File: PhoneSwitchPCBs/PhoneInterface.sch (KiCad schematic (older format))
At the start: 52 parts

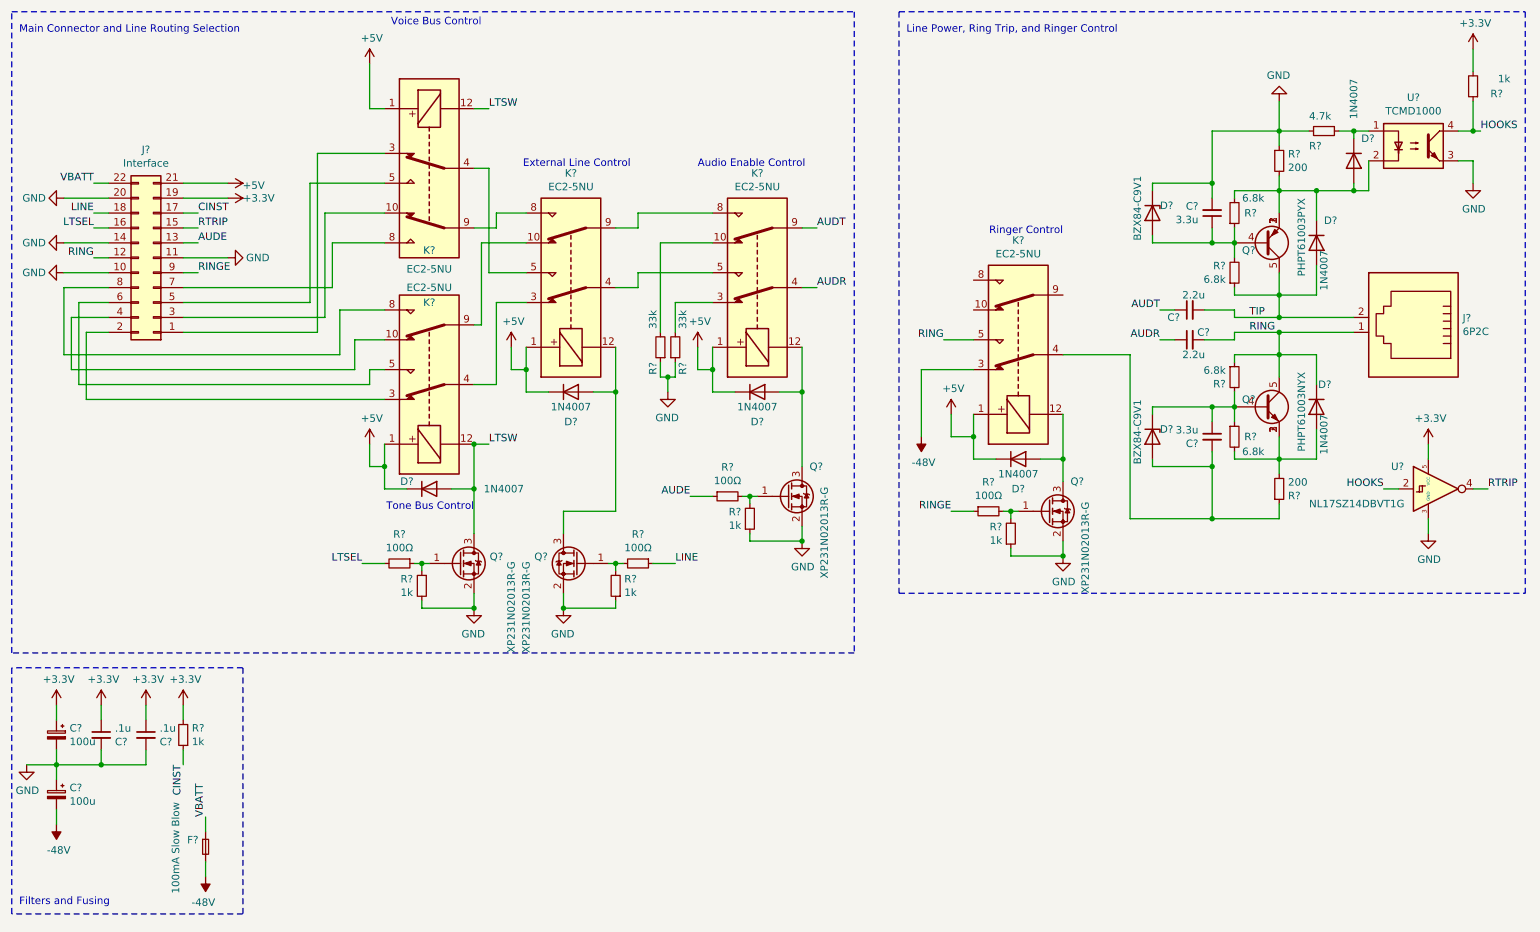
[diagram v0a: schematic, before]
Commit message: Update Notes, create custom footprint for RJ11 connector, associate footprints, fix cap types
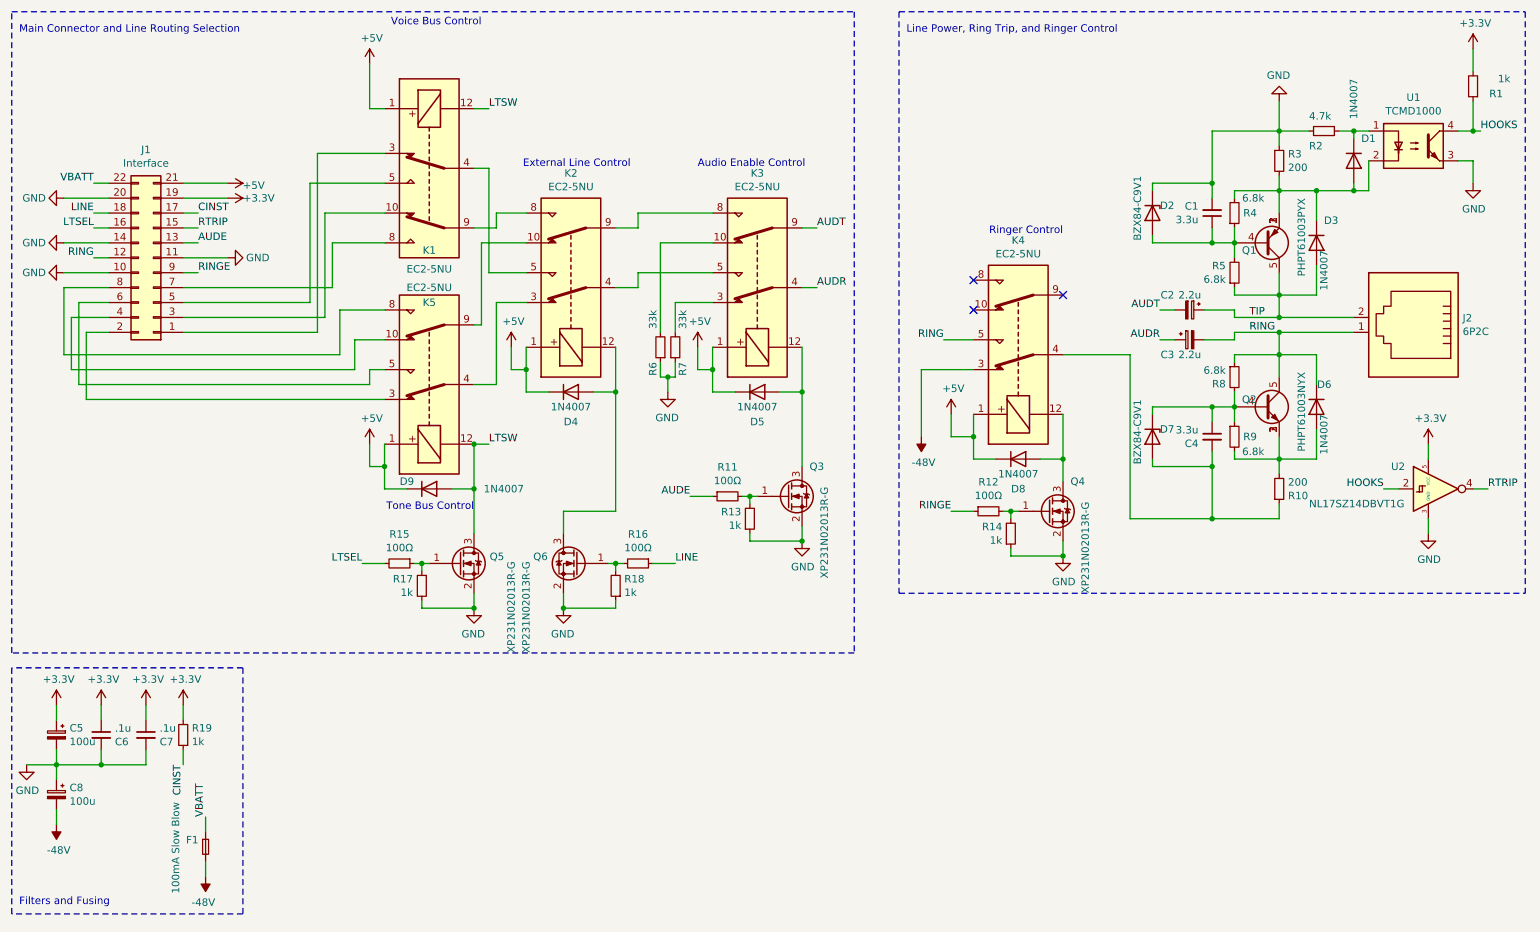
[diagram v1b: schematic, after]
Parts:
- removed C? (x2): 2.2u, symbol Device:C_Small
- added C2, C3: 2.2u, Capacitor_THT:CP_Radial_D4.0mm_P1.50mm, symbol Device:CP_Small
- C1, C4, C5: renamed from C?; footprint (none) -> Capacitor_THT:CP_Radial_D5.0mm_P2.00mm
- C8: renamed from C?; footprint (none) -> Capacitor_THT:CP_Radial_D10.0mm_P5.00mm
- F1: renamed from F?; footprint (none) -> Imported_Parts:00346605
- J1: renamed from J?; footprint (none) -> Connector_PinHeader_2.54mm:PinHeader_2x11_P2.54mm_Vertical
- J2: renamed from J?; footprint (none) -> PhoneInterfaceParts:RJE0112001
- R1, R13, R14, R17, R18, R19: renamed from R?; footprint (none) -> Resistor_SMD:R_0805_2012Metric_Pad1.20x1.40mm_HandSolder
- R4, R5, R8, R9: renamed from R?; footprint (none) -> Resistor_SMD:R_1210_3225Metric_Pad1.30x2.65mm_HandSolder
- gave numbers to parts that had none: 33
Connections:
- net AUDR: now also C3.1
- net AUDT: now also C2.2
- net RING: now also C3.2
- net TIP: now also C2.1
- no-connect marks 0 -> 3

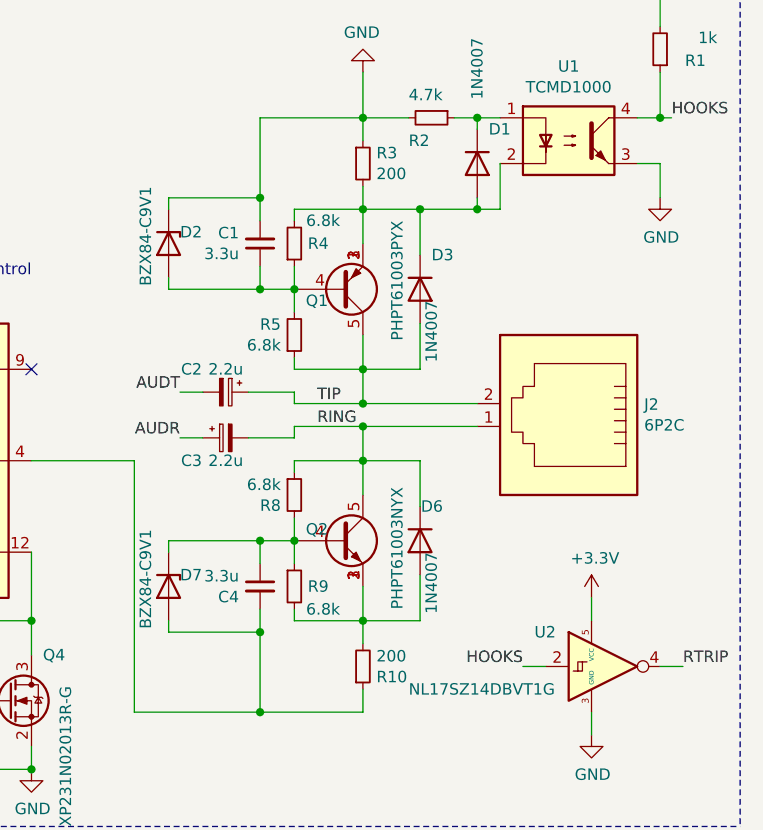
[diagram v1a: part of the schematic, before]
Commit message: Finished footprint associations
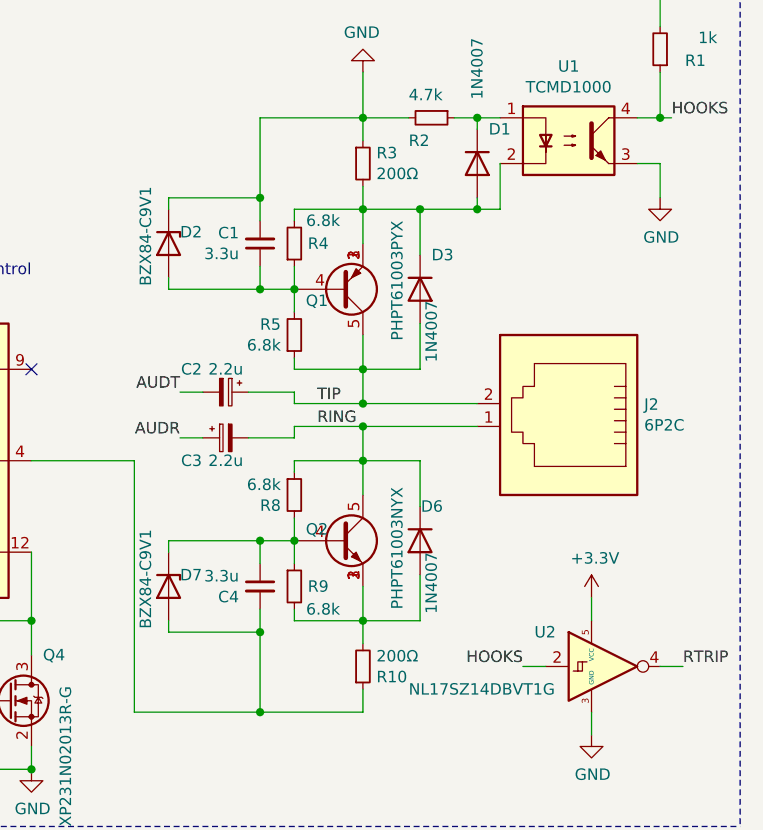
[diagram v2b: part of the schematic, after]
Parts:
- C6, C7: footprint (none) -> Capacitor_SMD:C_0603_1608Metric_Pad1.08x0.95mm_HandSolder
- R10, R3: value 200 -> 200Ω; footprint (none) -> Resistor_THT:R_Axial_DIN0516_L15.5mm_D5.0mm_P20.32mm_Horizontal
- R11, R12, R15, R16, R2, R6, R7: footprint (none) -> Resistor_SMD:R_0805_2012Metric_Pad1.20x1.40mm_HandSolder
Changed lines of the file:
@@
 P 9250 1650
 F 0 "R3" H 9309 1696 50  0000 L CNN
-F 1 "200" H 9309 1605 50  0000 L CNN
-F 2 "" H 9250 1650 50  0001 C CNN
+F 1 "200Ω" H 9309 1605 50  0000 L CNN
+F 2 "Resistor_THT:R_Axial_DIN0516_L15.5mm_D5.0mm_P20.32mm_Horizontal" H 9250 1650 50  0001 C CNN
 F 3 "~" H 9250 1650 50  0001 C CNN
 	1    9250 1650
@@
 P 9250 3850
 F 0 "R10" H 9309 3896 50  0000 L CNN
-F 1 "200" H 9309 3805 50  0000 L CNN
-F 2 "" H 9250 3850 50  0001 C CNN
+F 1 "200Ω" H 9309 3805 50  0000 L CNN
+F 2 "Resistor_THT:R_Axial_DIN0516_L15.5mm_D5.0mm_P20.32mm_Horizontal" H 9250 3850 50  0001 C CNN
 F 3 "~" H 9250 3850 50  0001 C CNN
 	1    9250 3850
@@
 F 0 "R2" V 9650 1350 50  0000 L CNN
 F 1 "4.7k" V 9450 1350 50  0000 L CNN
-F 2 "" H 9550 1450 50  0001 C CNN
+F 2 "Resistor_SMD:R_0805_2012Metric_Pad1.20x1.40mm_HandSolder" H 9550 1450 50  0001 C CNN
 F 3 "~" H 9550 1450 50  0001 C CNN
 	1    9550 1450
@@
 F 0 "R7" V 5250 3000 50  0000 L CNN
 F 1 "33k" V 5250 2650 50  0000 L CNN
-F 2 "" H 5200 2900 50  0001 C CNN
+F 2 "Resistor_SMD:R_0805_2012Metric_Pad1.20x1.40mm_HandSolder" H 5200 2900 50  0001 C CNN
 F 3 "~" H 5200 2900 50  0001 C CNN
 	1    5200 2900
@@
 F 0 "R6" V 5150 3000 50  0000 L CNN
 F 1 "33k" V 5150 2650 50  0000 L CNN
-F 2 "" H 5100 2900 50  0001 C CNN
+F 2 "Resistor_SMD:R_0805_2012Metric_Pad1.20x1.40mm_HandSolder" H 5100 2900 50  0001 C CNN
 F 3 "~" H 5100 2900 50  0001 C CNN
 	1    5100 2900
@@
 F 0 "R15" V 3154 4350 50  0000 C CNN
 F 1 "100Ω" V 3245 4350 50  0000 C CNN
-F 2 "" H 3350 4350 50  0001 C CNN
+F 2 "Resistor_SMD:R_0805_2012Metric_Pad1.20x1.40mm_HandSolder" H 3350 4350 50  0001 C CNN
 F 3 "~" H 3350 4350 50  0001 C CNN
 	1    3350 4350
@@
 F 0 "R16" V 4754 4350 50  0000 C CNN
 F 1 "100Ω" V 4845 4350 50  0000 C CNN
-F 2 "" H 4950 4350 50  0001 C CNN
+F 2 "Resistor_SMD:R_0805_2012Metric_Pad1.20x1.40mm_HandSolder" H 4950 4350 50  0001 C CNN
 F 3 "~" H 4950 4350 50  0001 C CNN
 	1    4950 4350
@@
 F 0 "R11" V 5354 3900 50  0000 C CNN
 F 1 "100Ω" V 5445 3900 50  0000 C CNN
-F 2 "" H 5550 3900 50  0001 C CNN
+F 2 "Resistor_SMD:R_0805_2012Metric_Pad1.20x1.40mm_HandSolder" H 5550 3900 50  0001 C CNN
 F 3 "~" H 5550 3900 50  0001 C CNN
 	1    5550 3900
@@
 F 0 "R12" V 7104 4000 50  0000 C CNN
 F 1 "100Ω" V 7195 4000 50  0000 C CNN
-F 2 "" H 7300 4000 50  0001 C CNN
+F 2 "Resistor_SMD:R_0805_2012Metric_Pad1.20x1.40mm_HandSolder" H 7300 4000 50  0001 C CNN
 F 3 "~" H 7300 4000 50  0001 C CNN
 	1    7300 4000
@@
 F 0 "C6" H 1258 5454 50  0000 R CNN
 F 1 ".1u" H 1258 5545 50  0000 R CNN
-F 2 "" H 1350 5500 50  0001 C CNN
+F 2 "Capacitor_SMD:C_0603_1608Metric_Pad1.08x0.95mm_HandSolder" H 1350 5500 50  0001 C CNN
 F 3 "~" H 1350 5500 50  0001 C CNN
 	1    1350 5500
@@
 F 0 "C7" H 1558 5454 50  0000 R CNN
 F 1 ".1u" H 1558 5545 50  0000 R CNN
-F 2 "" H 1650 5500 50  0001 C CNN
+F 2 "Capacitor_SMD:C_0603_1608Metric_Pad1.08x0.95mm_HandSolder" H 1650 5500 50  0001 C CNN
 F 3 "~" H 1650 5500 50  0001 C CNN
 	1    1650 5500
